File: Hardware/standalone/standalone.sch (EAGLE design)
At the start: 92 parts, among them IC1 STM32F050C6T6A, IC2 AP1212, Q2 32.768khz, U1 NMOS_2N7002, U10 ZXCT1107SA-7, U2 FDS6690a, U3 FDS6690a, U4 LM2576S, U5 NMOS_2N7002, U6 NMOS_2N7002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

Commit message: Moved drill holes to correct position
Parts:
- BUZZ1: device buzzer:BUZZ_14MM -> equinox:BUZZ_14MM; OC_FARNELL 1669967 -> (none)
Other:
- note removed: "Swap with 1192513"
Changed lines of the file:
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@@
 <attribute name="OC_FARNELL" value="1298246 "/>
 </part>
-<part name="BUZZ1" library="buzzer" deviceset="BUZZ_14MM" device="">
-<attribute name="OC_FARNELL" value="1669967"/>
-</part>
+<part name="BUZZ1" library="equinox" deviceset="BUZZ_14MM" device=""/>
 <part name="GND1" library="supply1" deviceset="GND" device="" value="GND"/>
 <part name="R_RST" library="rcl" deviceset="R-EU_" device="M0805" value="100K"/>
@@
 <text x="355.6" y="426.72" size="1.778" layer="98">Add PTC: 1800724
 And Diode</text>
-<text x="274.32" y="96.52" size="1.778" layer="98" rot="R90">Swap with 1192513</text>
 </plain>
 <instances>

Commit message: Latest V2.4 PCB design (Sent to EuroCircuits)
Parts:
- removed GATE_DRIVE: IR2104S, equinox:IR2104S
- removed R1: 1k, resistor:R-EU_M0805
- removed U1: NMOS_2N7002, equinox:NMOS_2N7002
- added C16: 1uF, resistor:C-EUC0805K
- added D1: SSB43L, equinox:DIODE_SSB43L
- added D5: BZX384-C3V6, equinox:BZX384-C3V6
- added IC3: IR2104S, equinox:IR2104S
- added PTC1: 7A, equinox:PTC_MF_R700
- added R31: 10M, resistor:R-EU_M0805
- added U11, U12: NMOS_2N7002, equinox:NMOS_2N7002
- renumbered 5V_CIN to C21, 5V_COUT to C22, Q2 to Q1, U$2 to DC3, U$3 to DC2, U$4 to DC1
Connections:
- removed net LCD_PWR: IC1.PA11, R1.2
- removed net N$17: R1.1, U1.G
- removed net N$5: CONTR.E, DIS1.D0, DIS1.D1, DIS1.D2, DIS1.D3, DIS1.GND, U1.D
- new net N$44: C16.2, R31.2, U11.G
- new net N$45: U11.D, U12.S
- new net N$46: BATTCON$1.S, PTC1.P$2
- net GND: now also C16.1, CONTR.E, D1.ANODE, D5.A, DIS1.D0, DIS1.D1, DIS1.D2, DIS1.D3, DIS1.GND, IC3.COM, U11.S; no longer GATE_DRIVE.COM, U1.S
- net N$10: now also IC3.VB; no longer GATE_DRIVE.VB
- net N$13: now also IC3.LO; no longer GATE_DRIVE.LO
- net N$16: now also IC3.VCC; no longer GATE_DRIVE.VCC
- net N$3: now also IC3.SD/; no longer GATE_DRIVE.SD/
- net N$4: now also D1.CATHODE, PTC1.P$1; no longer BATTCON$1.S
- net N$6: now also IC3.VS; no longer GATE_DRIVE.VS
- net N$7: now also IC3.HO; no longer GATE_DRIVE.HO
- net N$8: now also IC3.IN; no longer GATE_DRIVE.IN
- net NRST: now also U12.D
- net SOL_I: now also D5.C
- net WKUP: now also R31.1, U12.G
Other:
- note added: "TODO: - Contrast Adjust Pot needs changing - Swap MOS with BJT - Remove LCD Switching"
- note removed: "Add PTC: 1800724 And Diode"
- note removed: "TODO: - Contrast Adjust Pot needs changing - Add PTC & Diode"
- moved on the sheet: BATTCON$1, BATTCON$2, C11, C19, C2, C20, C3, C5, C6, C8, D2, D3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

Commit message: Clean up of Hardware folder
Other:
- note added: "TODO: - Contrast Adjust Pot needs changing - Swap MOS with BJT"
- note removed: "TODO: - Contrast Adjust Pot needs changing - Swap MOS with BJT - Remove LCD Switching"
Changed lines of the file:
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@@
 <text x="406.4" y="502.92" size="3.81" layer="98" rot="MR180">TODO:
   - Contrast Adjust Pot needs changing
-  - Swap MOS with BJT
-  - Remove LCD Switching</text>
+  - Swap MOS with BJT</text>
 <text x="662.94" y="127" size="1.778" layer="98">0.5A Current Limit</text>
 <text x="662.94" y="86.36" size="1.778" layer="98">0.5A Current Limit</text>

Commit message: Parallel Resistor added to buzzer circuit.
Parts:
- added R1: 100, resistor:R-EU_M0805
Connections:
- net N$42: now also R1.2
- net V_LOAD: now also R1.1
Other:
- note added: "Hardware Reset Timer"
- note added: "TODO: - Contrast Adjust Pot needs changing - Swap MOS with BJT - Change XTAL to new 6pF"
- note removed: "TODO: - Contrast Adjust Pot needs changing - Swap MOS with BJT"
- moved on the sheet: D1, R31
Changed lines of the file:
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@@
 </part>
 <part name="D5" library="equinox" deviceset="BZX384-C3V6" device=""/>
+<part name="R1" library="resistor" deviceset="R-EU_" device="M0805" value="100"/>
 </parts>
 <sheets>
@@
 <text x="406.4" y="502.92" size="3.81" layer="98" rot="MR180">TODO:
   - Contrast Adjust Pot needs changing
-  - Swap MOS with BJT</text>
+  - Swap MOS with BJT
+  - Change XTAL to new 6pF</text>
 <text x="662.94" y="127" size="1.778" layer="98">0.5A Current Limit</text>
 <text x="662.94" y="86.36" size="1.778" layer="98">0.5A Current Limit</text>
@@
 <text x="556.26" y="132.08" size="1.778" layer="98" rot="R90">250mA Output</text>
 <text x="297.18" y="66.04" size="1.778" layer="98">Must be placed near to IC1</text>
+<wire x1="125.222" y1="77.47" x2="72.898" y2="77.47" width="0.1524" layer="98"/>
+<wire x1="72.898" y1="77.47" x2="72.898" y2="34.798" width="0.1524" layer="98"/>
+<wire x1="72.898" y1="34.798" x2="125.222" y2="34.798" width="0.1524" layer="98"/>
+<wire x1="125.222" y1="34.798" x2="125.222" y2="77.47" width="0.1524" layer="98"/>
+<text x="73.66" y="78.74" size="1.778" layer="98">Hardware Reset Timer</text>
 </plain>
 <instances>
@@
 <instance part="R29" gate="G$1" x="248.92" y="96.52" rot="R270"/>
 <instance part="GND9" gate="1" x="60.96" y="30.48"/>
-<instance part="R31" gate="G$1" x="83.82" y="71.12" rot="R270"/>
+<instance part="R31" gate="G$1" x="83.82" y="60.96" rot="R270"/>
 <instance part="C16" gate="G$1" x="83.82" y="38.1" rot="R180"/>
 <instance part="GND18" gate="1" x="83.82" y="30.48"/>
@@
 <instance part="GND31" gate="1" x="114.3" y="30.48"/>
 <instance part="PTC1" gate="PTC1" x="363.22" y="424.18"/>
-<instance part="D1" gate="1" x="358.14" y="398.78" rot="R90">
-<attribute name="OC_FARNELL" x="358.14" y="398.78" size="1.778" layer="96" rot="R90" display="off"/>
+<instance part="D1" gate="1" x="358.14" y="393.7" rot="R90">
+<attribute name="OC_FARNELL" x="358.14" y="393.7" size="1.778" layer="96" rot="R90" display="off"/>
 </instance>
 <instance part="D5" gate="1" x="60.96" y="398.78" rot="R90"/>
+<instance part="R1" gate="G$1" x="279.4" y="109.22" rot="R270"/>
 </instances>
 <busses>
@@
 <pinref part="PTC1" gate="PTC1" pin="P$1"/>
 <pinref part="D1" gate="1" pin="CATHODE"/>
-<wire x1="358.14" y1="403.86" x2="358.14" y2="424.18" width="0.1524" layer="91"/>
+<wire x1="358.14" y1="398.78" x2="358.14" y2="424.18" width="0.1524" layer="91"/>
 <junction x="358.14" y="424.18"/>
 </segment>
@@
 <segment>
 <pinref part="BUZZ1" gate="G$1" pin="+"/>
-<wire x1="259.08" y1="114.3" x2="259.08" y2="129.54" width="0.1524" layer="91"/>
+<wire x1="259.08" y1="114.3" x2="259.08" y2="121.92" width="0.1524" layer="91"/>
+<wire x1="259.08" y1="121.92" x2="259.08" y2="129.54" width="0.1524" layer="91"/>
 <wire x1="259.08" y1="129.54" x2="276.86" y2="129.54" width="0.1524" layer="91"/>
 <label x="264.16" y="129.54" size="1.778" layer="95"/>
+<pinref part="R1" gate="G$1" pin="1"/>
+<wire x1="279.4" y1="114.3" x2="279.4" y2="121.92" width="0.1524" layer="91"/>
+<wire x1="279.4" y1="121.92" x2="259.08" y2="121.92" width="0.1524" layer="91"/>
+<junction x="259.08" y="121.92"/>
 </segment>
 </net>
@@
 <wire x1="83.82" y1="99.06" x2="101.6" y2="99.06" width="0.1524" layer="91"/>
 <wire x1="101.6" y1="99.06" x2="139.7" y2="99.06" width="0.1524" layer="91"/>
-<wire x1="83.82" y1="76.2" x2="83.82" y2="99.06" width="0.1524" layer="91"/>
+<wire x1="83.82" y1="66.04" x2="83.82" y2="99.06" width="0.1524" layer="91"/>
 <junction x="83.82" y="99.06"/>
 <pinref part="U12" gate="A" pin="G"/>
@@
 <junction x="297.18" y="342.9"/>
 <pinref part="D1" gate="1" pin="ANODE"/>
-<wire x1="358.14" y1="393.7" x2="358.14" y2="342.9" width="0.1524" layer="91"/>
+<wire x1="358.14" y1="388.62" x2="358.14" y2="342.9" width="0.1524" layer="91"/>
 <junction x="358.14" y="342.9"/>
 <pinref part="D5" gate="1" pin="A"/>
@@
 <pinref part="U8" gate="A" pin="D"/>
 <pinref part="BUZZ1" gate="G$1" pin="-"/>
-<wire x1="259.08" y1="91.44" x2="259.08" y2="106.68" width="0.1524" layer="91"/>
+<wire x1="259.08" y1="91.44" x2="259.08" y2="101.6" width="0.1524" layer="91"/>
+<pinref part="R1" gate="G$1" pin="2"/>
+<wire x1="259.08" y1="101.6" x2="259.08" y2="106.68" width="0.1524" layer="91"/>
+<wire x1="279.4" y1="104.14" x2="279.4" y2="101.6" width="0.1524" layer="91"/>
+<wire x1="279.4" y1="101.6" x2="259.08" y2="101.6" width="0.1524" layer="91"/>
+<junction x="259.08" y="101.6"/>
 </segment>
 </net>
@@
 <pinref part="R31" gate="G$1" pin="2"/>
 <pinref part="C16" gate="G$1" pin="2"/>
-<wire x1="83.82" y1="43.18" x2="83.82" y2="66.04" width="0.1524" layer="91"/>
+<wire x1="83.82" y1="43.18" x2="83.82" y2="55.88" width="0.1524" layer="91"/>
 <wire x1="83.82" y1="43.18" x2="104.14" y2="43.18" width="0.1524" layer="91"/>
 <junction x="83.82" y="43.18"/>

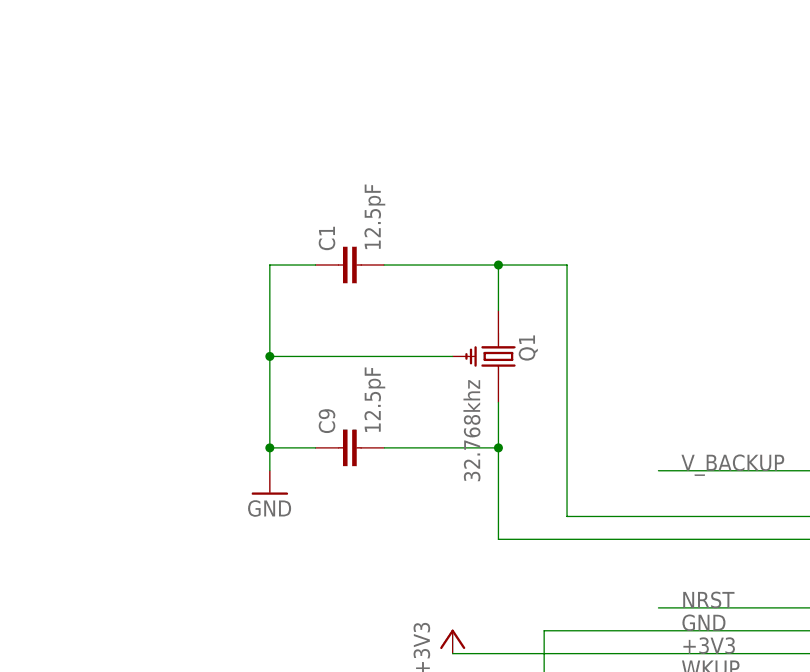
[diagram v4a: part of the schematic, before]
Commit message: Changed RTC XTAL Hardware
Both Home and Pro boards have working XTAL. OC_FARNELL attributes give
correct part numbers.
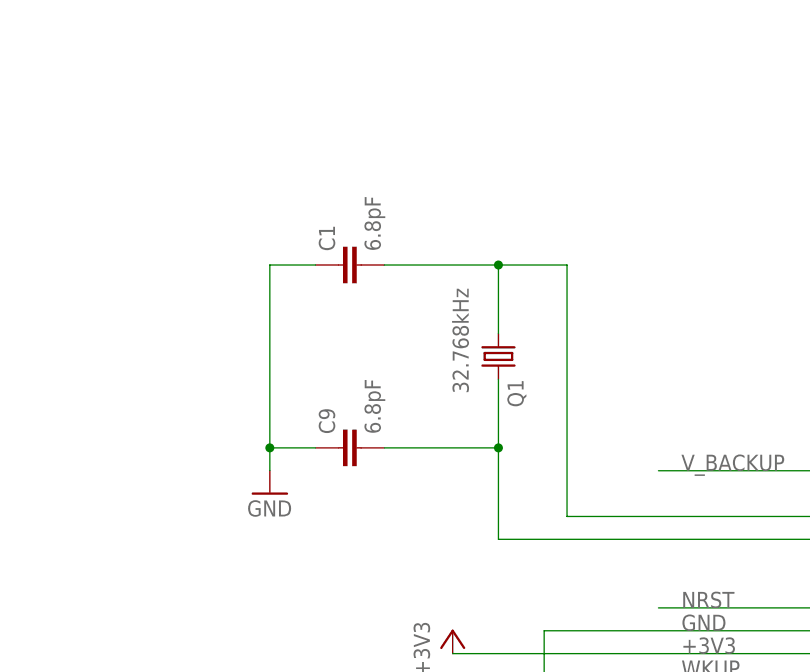
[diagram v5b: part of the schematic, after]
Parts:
- C1, C9: value 12.5pF -> 6.8pF; device resistor:C-EUC0805K -> resistor:C-EUC0603K; OC_FARNELL (none) -> 1856141
- Q1: value 32.768khz -> 32.768kHz; device equinox:CRYSTAL_CMJ206T -> crystal:MC-306; MPN (none) -> MC-306; OC_FARNELL 2101358 -> 1712823; OC_NEWARK (none) -> -
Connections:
- net GND: no longer Q1.P$1
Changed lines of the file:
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@@
 <part name="GND11" library="supply1" deviceset="GND" device="" value="GND"/>
 <part name="GND13" library="supply1" deviceset="GND" device="" value="GND"/>
-<part name="Q1" library="equinox" deviceset="CRYSTAL_CMJ206T" device="" value="32.768khz">
-<attribute name="OC_FARNELL" value="2101358"/>
-</part>
-<part name="C1" library="resistor" deviceset="C-EU" device="C0805K" value="12.5pF"/>
-<part name="C9" library="resistor" deviceset="C-EU" device="C0805K" value="12.5pF"/>
+<part name="C1" library="resistor" deviceset="C-EU" device="C0603K" value="6.8pF">
+<attribute name="OC_FARNELL" value="1856141"/>
+</part>
+<part name="C9" library="resistor" deviceset="C-EU" device="C0603K" value="6.8pF">
+<attribute name="OC_FARNELL" value="1856141"/>
+</part>
 <part name="GND14" library="supply1" deviceset="GND" device="" value="GND"/>
 <part name="+3V5" library="supply1" deviceset="+3V3" device=""/>
@@
 <part name="D5" library="equinox" deviceset="BZX384-C3V6" device=""/>
 <part name="R1" library="resistor" deviceset="R-EU_" device="M0805" value="100"/>
+<part name="Q1" library="crystal" deviceset="MC-306" device="" value="32.768kHz">
+<attribute name="MPN" value="MC-306"/>
+<attribute name="OC_FARNELL" value="1712823"/>
+<attribute name="OC_NEWARK" value="-"/>
+</part>
 </parts>
 <sheets>
@@
 <instance part="GND11" gate="1" x="132.08" y="111.76"/>
 <instance part="GND13" gate="1" x="170.18" y="167.64"/>
-<instance part="Q1" gate="G$1" x="127" y="149.86" rot="R270">
-<attribute name="OC_FARNELL" x="127" y="149.86" size="1.778" layer="96" rot="R270" display="off"/>
-</instance>
-<instance part="C1" gate="G$1" x="109.22" y="160.02" rot="R90"/>
-<instance part="C9" gate="G$1" x="109.22" y="139.7" rot="R90"/>
+<instance part="C1" gate="G$1" x="109.22" y="160.02" rot="R90">
+<attribute name="OC_FARNELL" x="109.22" y="160.02" size="1.778" layer="96" rot="R90" display="off"/>
+</instance>
+<instance part="C9" gate="G$1" x="109.22" y="139.7" rot="R90">
+<attribute name="OC_FARNELL" x="109.22" y="139.7" size="1.778" layer="96" rot="R90" display="off"/>
+</instance>
 <instance part="GND14" gate="1" x="101.6" y="134.62"/>
 <instance part="+3V5" gate="G$1" x="294.64" y="60.96"/>
@@
 <instance part="D5" gate="1" x="60.96" y="398.78" rot="R90"/>
 <instance part="R1" gate="G$1" x="279.4" y="109.22" rot="R270"/>
+<instance part="Q1" gate="P" x="127" y="149.86" smashed="yes" rot="R270">
+<attribute name="NAME" x="128.016" y="147.32" size="1.778" layer="95" rot="R270"/>
+<attribute name="VALUE" x="121.92" y="157.48" size="1.778" layer="96" rot="R270"/>
+</instance>
 </instances>
 <busses>
@@
 <wire x1="162.56" y1="132.08" x2="134.62" y2="132.08" width="0.1524" layer="91"/>
 <wire x1="134.62" y1="132.08" x2="134.62" y2="160.02" width="0.1524" layer="91"/>
-<pinref part="Q1" gate="G$1" pin="1"/>
-<wire x1="127" y1="154.94" x2="127" y2="160.02" width="0.1524" layer="91"/>
+<pinref part="C1" gate="G$1" pin="2"/>
 <wire x1="134.62" y1="160.02" x2="127" y2="160.02" width="0.1524" layer="91"/>
-<pinref part="C1" gate="G$1" pin="2"/>
+<pinref part="Q1" gate="P" pin="1"/>
 <wire x1="127" y1="160.02" x2="114.3" y2="160.02" width="0.1524" layer="91"/>
+<wire x1="127" y1="152.4" x2="127" y2="160.02" width="0.1524" layer="91"/>
 <junction x="127" y="160.02"/>
 </segment>
@@
 <segment>
 <pinref part="IC1" gate="1" pin="PC15_OSC32_OUT"/>
-<pinref part="Q1" gate="G$1" pin="2"/>
 <wire x1="162.56" y1="129.54" x2="127" y2="129.54" width="0.1524" layer="91"/>
 <wire x1="127" y1="129.54" x2="127" y2="139.7" width="0.1524" layer="91"/>
 <pinref part="C9" gate="G$1" pin="2"/>
-<wire x1="127" y1="139.7" x2="127" y2="144.78" width="0.1524" layer="91"/>
 <wire x1="114.3" y1="139.7" x2="127" y2="139.7" width="0.1524" layer="91"/>
+<pinref part="Q1" gate="P" pin="2"/>
+<wire x1="127" y1="147.32" x2="127" y2="139.7" width="0.1524" layer="91"/>
 <junction x="127" y="139.7"/>
 </segment>
@@
 <wire x1="101.6" y1="137.16" x2="101.6" y2="139.7" width="0.1524" layer="91"/>
 <pinref part="C1" gate="G$1" pin="1"/>
-<wire x1="101.6" y1="139.7" x2="101.6" y2="149.86" width="0.1524" layer="91"/>
-<wire x1="101.6" y1="149.86" x2="101.6" y2="160.02" width="0.1524" layer="91"/>
+<wire x1="101.6" y1="139.7" x2="101.6" y2="160.02" width="0.1524" layer="91"/>
 <wire x1="101.6" y1="160.02" x2="106.68" y2="160.02" width="0.1524" layer="91"/>
 <pinref part="C9" gate="G$1" pin="1"/>
 <wire x1="106.68" y1="139.7" x2="101.6" y2="139.7" width="0.1524" layer="91"/>
 <junction x="101.6" y="139.7"/>
-<pinref part="Q1" gate="G$1" pin="P$1"/>
-<wire x1="121.92" y1="149.86" x2="101.6" y2="149.86" width="0.1524" layer="91"/>
-<junction x="101.6" y="149.86"/>
-</segment>
-<segment>
+</segment>
+<segment>
